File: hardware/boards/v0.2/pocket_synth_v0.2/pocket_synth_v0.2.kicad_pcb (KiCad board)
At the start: 6 copper layers, 155 x 162 mm, 54 parts, among them J1 Conn_ARM_JTAG_SWD_10, J2 DEVICE, J3 AudioJack3, J4 AudioJack3, J5 AudioJack3, J6 AudioJack3, J7 DISPLAY, J8 Micro_SD_Card_Det2, J9 HOST, SW1 SW_Push, SW2 SW_Push, SW3 SW_Push, SW4 SW_Push, U1 STM32H743XIHx, U3 SDRAM, U4 STM32H753VIHx, U5 W25Q128JVS, Y1 32.768kHz, Y2 HSE

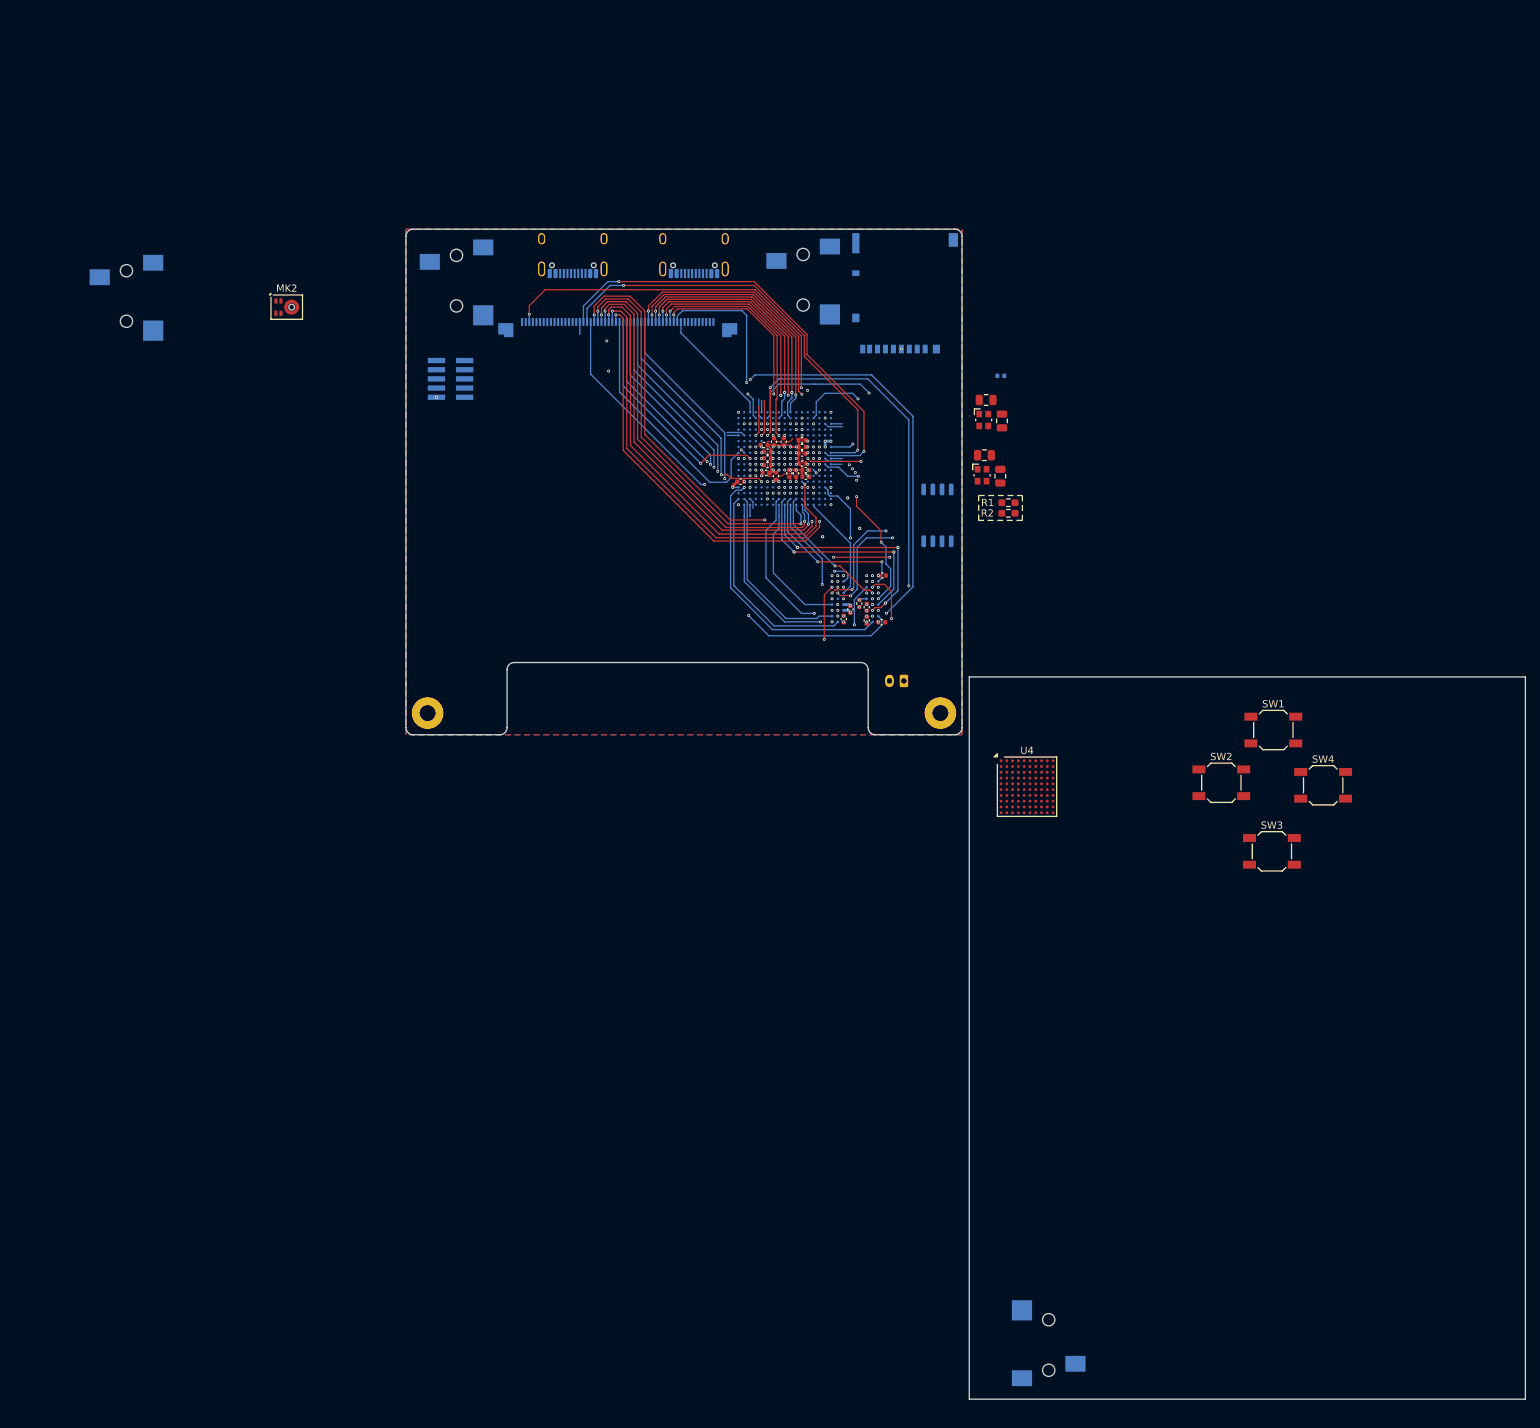
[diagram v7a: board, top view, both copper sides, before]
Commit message: routing of various peripherals
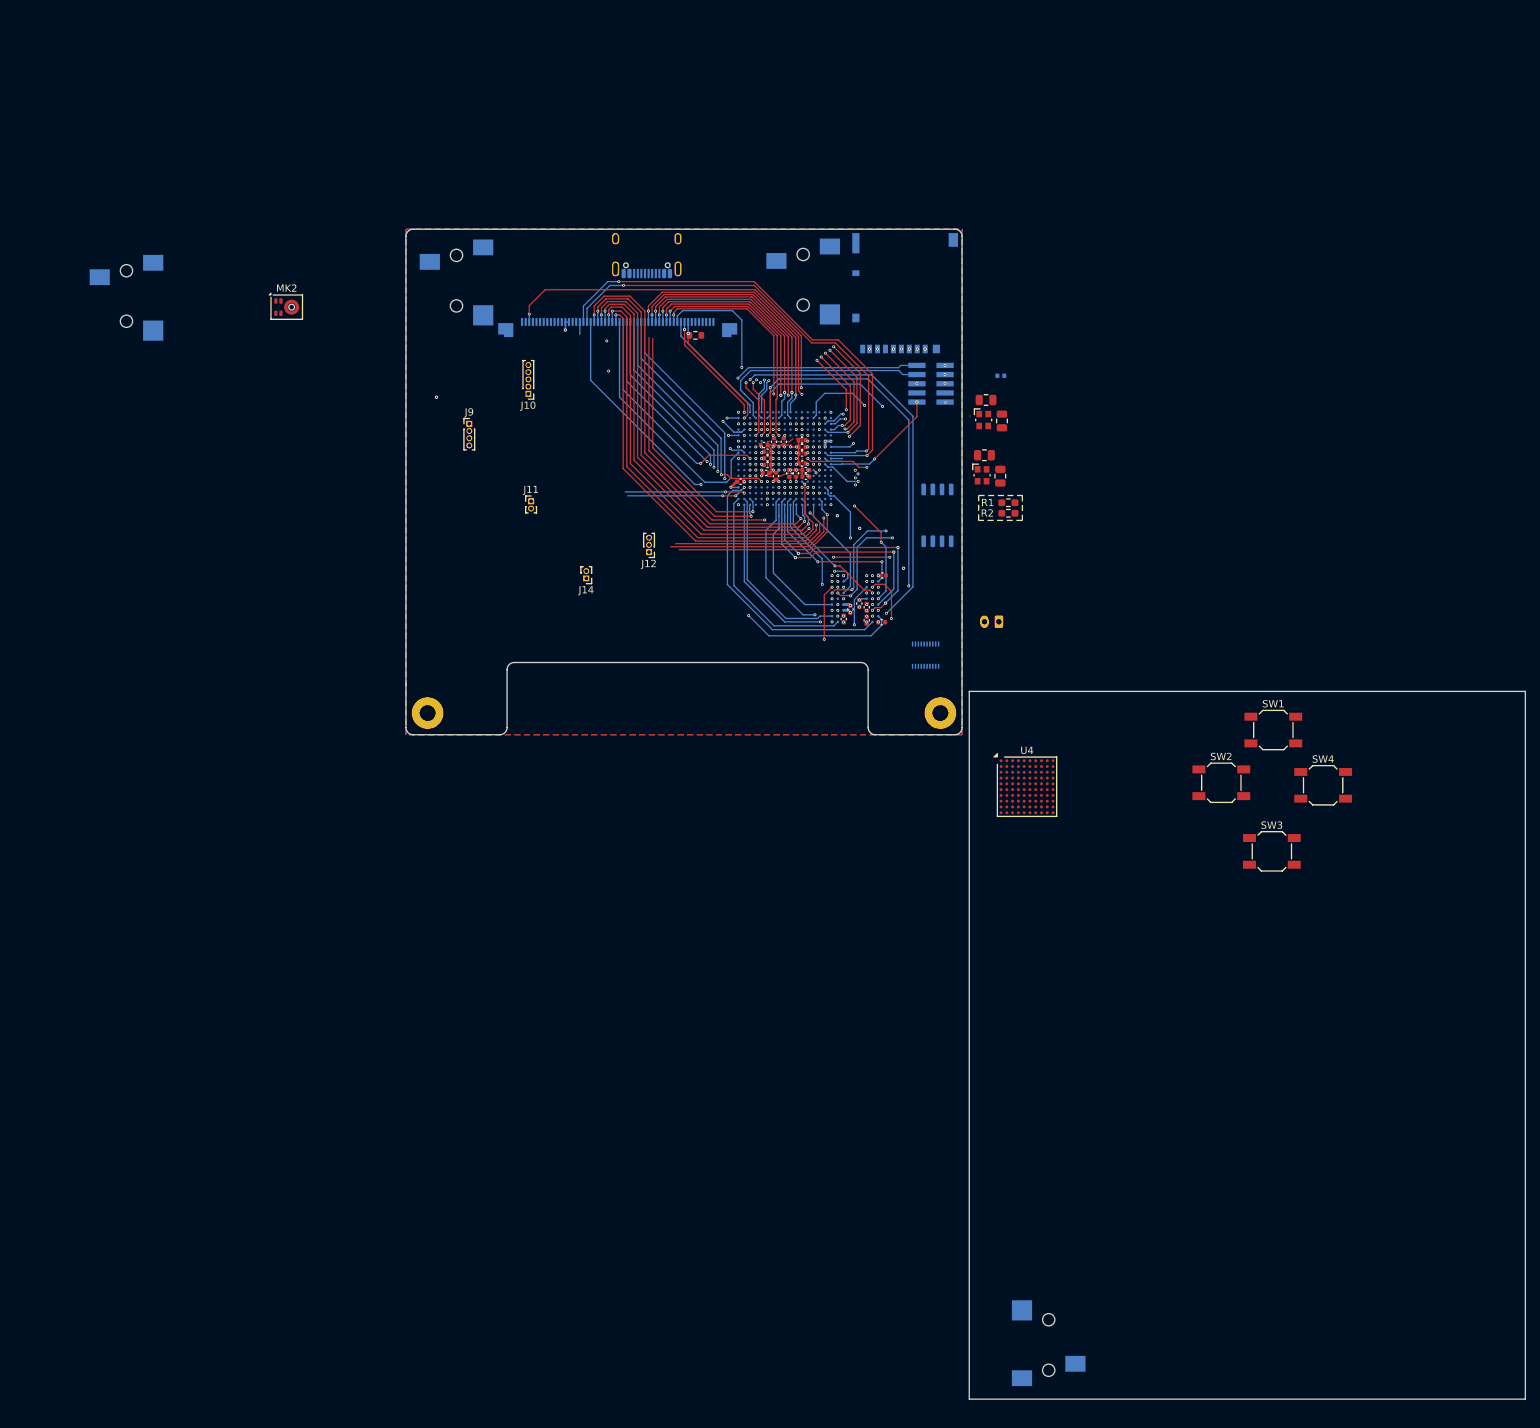
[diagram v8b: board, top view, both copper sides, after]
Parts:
- added J10: Conn_01x05_Pin, Connector_PinHeader_1.00mm:PinHeader_1x05_P1.00mm_Vertical, F.Cu at (28.9, 34.8)
- added J11: Conn_01x02_Pin, Connector_PinHeader_1.00mm:PinHeader_1x02_P1.00mm_Vertical, F.Cu at (29.3, 49.7)
- added J12: Conn_01x03_Pin, Connector_PinHeader_1.00mm:PinHeader_1x03_P1.00mm_Vertical, F.Cu at (45.7, 56.7)
- added J13: INPUT, Connector_Hirose_DF40:Hirose_DF40C-20DS-0.4V_2x10_P0.4mm, B.Cu at (84.0, 71.0)
- added J14: UART4, Connector_PinHeader_1.00mm:PinHeader_1x02_P1.00mm_Vertical, F.Cu at (37.0, 60.4)
- added R3: R, Resistor_SMD:R_0603_1608Metric, F.Cu at (52.1, 26.7)
- J2: value DEVICE -> USB
- J9: value HOST -> USART4; footprint Connector_USB:USB_C_Receptacle_HCTL_HC-TYPE-C-16P-01A -> Connector_PinHeader_1.00mm:PinHeader_1x04_P1.00mm_Vertical; moved to F.Cu
- moved J1 66.5 mm to (84.7, 33.4), turned to 180 degrees
- moved J9 39.6 mm to (20.8, 39.0)
- moved BT1 15.5 mm to (94.1, 66.3)
- moved J2 10.2 mm to (45.4, 14.4)
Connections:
- H1 pad 1: unconnected-(H1-Pad1) -> GND
- H2 pad 1: unconnected-(H2-Pad1) -> GND
- J7 pad 41: unconnected-(J7-Pin_41-Pad41) -> +3.3V
- J7 pad 42: unconnected-(J7-Pin_42-Pad42) -> +3.3V
- U1 pad A16: unconnected-(U1-PI0-PadA16) -> /LCD_SPI_CS
- U1 pad B16: unconnected-(U1-PH15-PadB16) -> /LCD_RESET
- U1 pad B17: unconnected-(U1-PH14-PadB17) -> Net-(J14-Pin_2)
- U1 pad B5: unconnected-(U1-PB6-PadB5) -> /QSPI1_CS
- U1 pad C3: unconnected-(U1-PE2-PadC3) -> /SAI1_MCLK_A
- U1 pad D1: unconnected-(U1-PE5-PadD1) -> /SAI1_SCK_A
- U1 pad D14: unconnected-(U1-PA10-PadD14) -> Net-(J9-Pin_2)
- U1 pad D15: unconnected-(U1-PA9-PadD15) -> Net-(J9-Pin_1)
- U1 pad D16: unconnected-(U1-PH13-PadD16) -> Net-(J14-Pin_1)
- U1 pad D2: unconnected-(U1-PE4-PadD2) -> /SAI1_FS_A
- U1 pad D3: unconnected-(U1-PE3-PadD3) -> /SAI1_SD_B
- U1 pad E16: /USB_FS_D+ -> Net-(J9-Pin_4)
- U1 pad E17: /USB_FS_D- -> Net-(J9-Pin_3)
- U1 pad E5: unconnected-(U1-PE6-PadE5) -> /SAI1_SD_A
- U1 pad G15: /QSPI1_CS -> unconnected-(U1-PG6-PadG15)
- U1 pad R16: unconnected-(U1-PD12-PadR16) -> /I2C4_SCL
- U1 pad R17: unconnected-(U1-PD13-PadR17) -> /I2C4_SDA
- U1 pad R3: unconnected-(U1-PA6-PadR3) -> /SPI1_MISO
- U1 pad R5: unconnected-(U1-PA7-PadR5) -> /SPI1_MOSI
- U1 pad T3: unconnected-(U1-PA5-PadT3) -> /SPI1_SCK
- U1 pad U3: /MEM_SELECT -> unconnected-(U1-PA4-PadU3)
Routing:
- net /SAI1_SD_A: track 0.00 -> 57.2 mm, vias 0 -> 3
- net /SAI1_FS_A: track 0.00 -> 53.6 mm, vias 0 -> 2
- net /SAI1_SD_B: track 0.00 -> 50.9 mm, vias 0 -> 3
- net /SAI1_SCK_A: track 0.00 -> 47.1 mm, vias 0 -> 2
- net /SAI1_MCLK_A: track 0.00 -> 46.4 mm, vias 0 -> 3
- net Net-(J9-Pin_2): track 0.00 -> 34.5 mm, vias 0 -> 1
- net /USB_HS_D-: track 1.59 -> 35.3 mm, vias 0 -> 1
- net Net-(J9-Pin_1): track 0.00 -> 33.2 mm, vias 0 -> 1
- net Net-(J9-Pin_4): track 0.00 -> 33.2 mm, vias 0 -> 1
- net /USB_HS_D+: track 1.49 -> 34.6 mm, vias 0 -> 1
- net Net-(J9-Pin_3): track 0.00 -> 33.1 mm, vias 0 -> 1
- net /SPI1_MISO: track 0.00 -> 27.6 mm, vias 0 -> 2
- net /SPI1_MOSI: track 0.00 -> 27.1 mm, vias 0 -> 2
- net /SDMMC1_D2: track 1.61 -> 28.3 mm, vias 0 -> 2
- net /SPI1_SCK: track 0.00 -> 26.5 mm, vias 0 -> 1
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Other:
- outline, holes or cut-outs redrawn
- board text added: "WIFI NORA-W40"
- board text removed: "Longest SDRAM trace is 60mm, aim for all traces to have ~20mm skew."
